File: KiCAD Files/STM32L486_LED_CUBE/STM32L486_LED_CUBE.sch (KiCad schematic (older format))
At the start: 0 parts

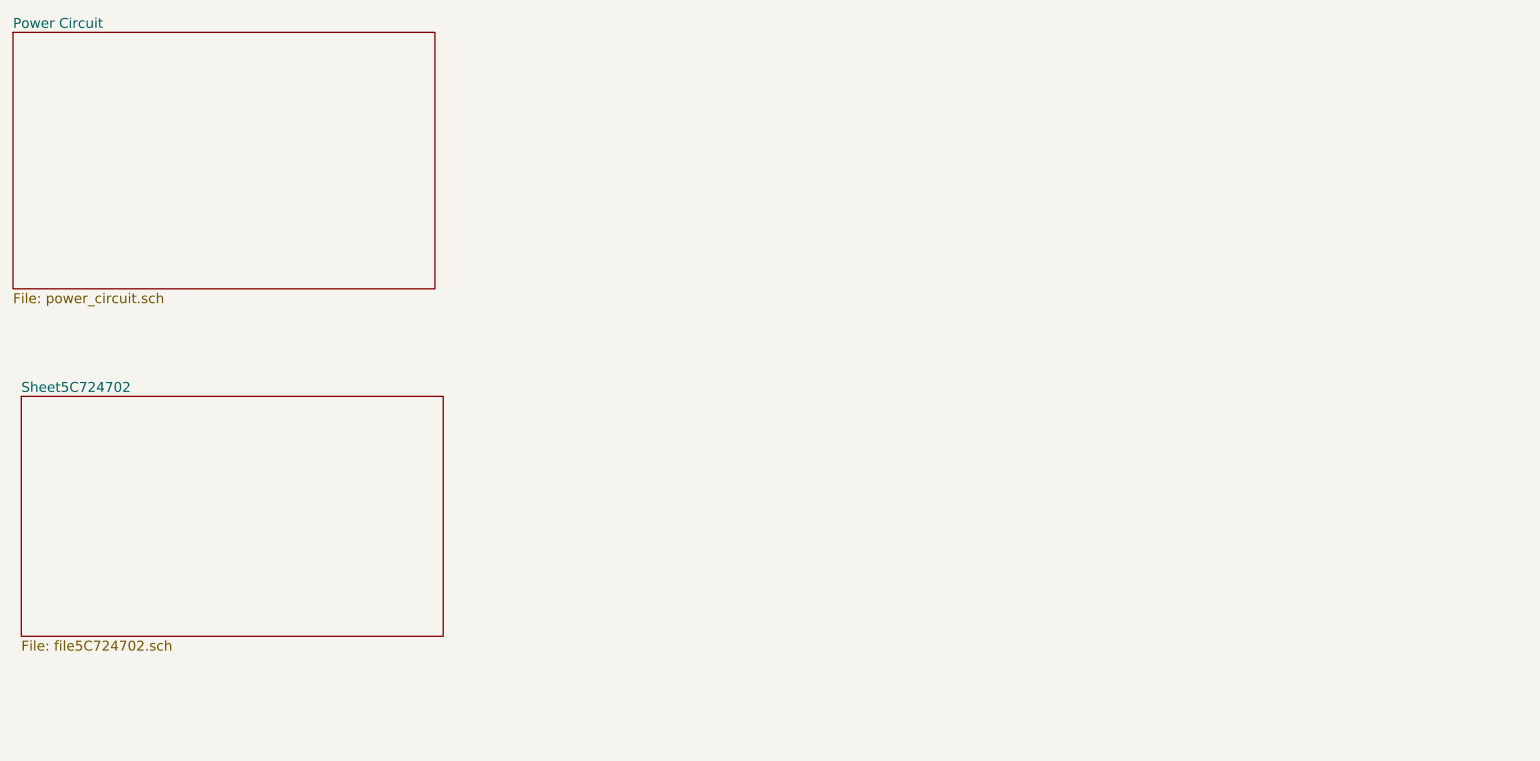
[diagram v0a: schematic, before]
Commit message: Updated KiCAD schematic. TLC portion added.
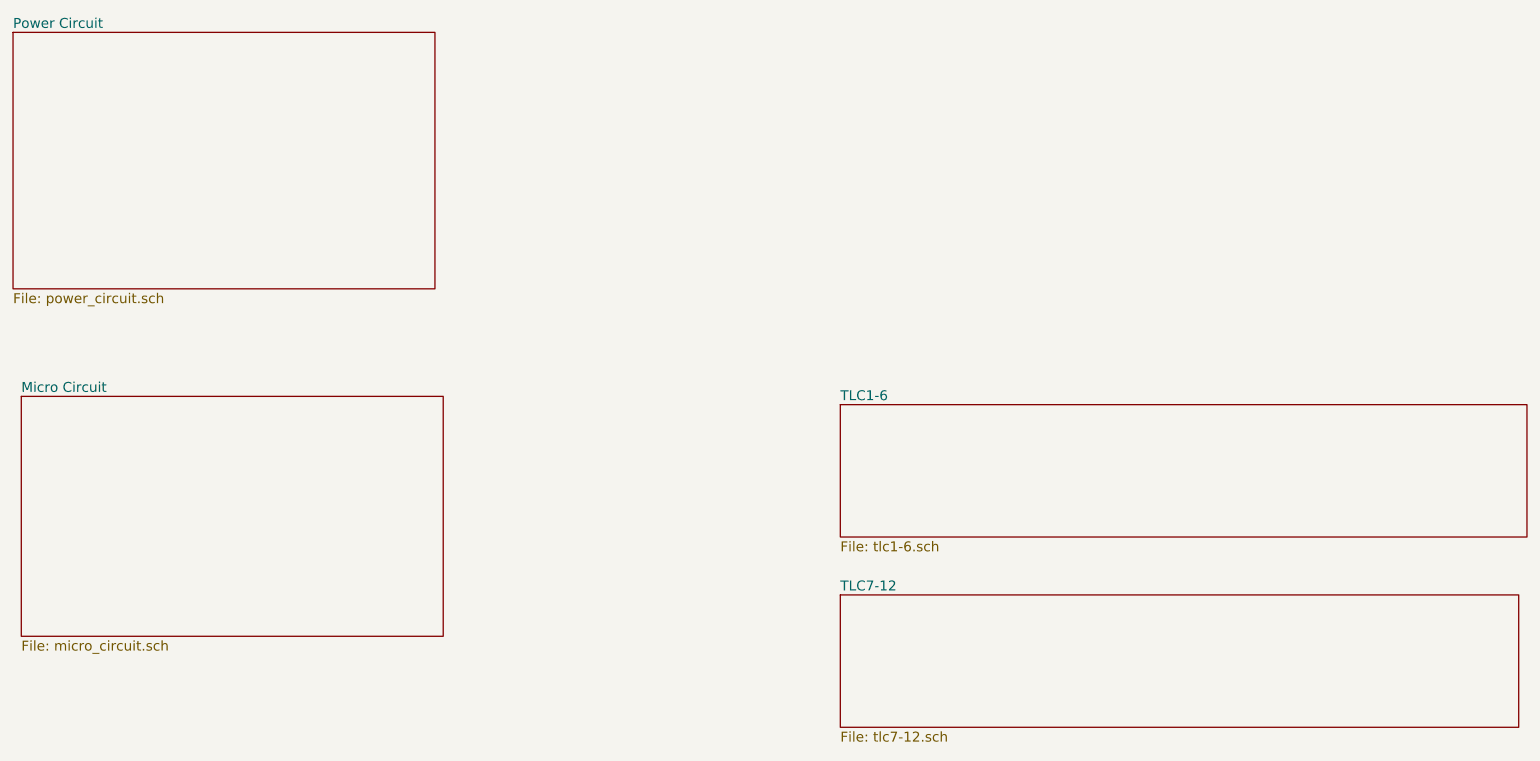
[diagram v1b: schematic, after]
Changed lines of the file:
@@
 $Descr A4 11693 8268
 encoding utf-8
-Sheet 1 3
+Sheet 1 5
 Title ""
 Date ""
@@
 S 1700 3300 2550 1450
 U 5C724703
-F0 "Sheet5C724702" 60
-F1 "file5C724702.sch" 60
+F0 "Micro Circuit" 60
+F1 "micro_circuit.sch" 60
+$EndSheet
+$Sheet
+S 6650 3350 4150 800
+U 5C733F59
+F0 "TLC1-6" 60
+F1 "tlc1-6.sch" 60
+$EndSheet
+$Sheet
+S 6650 4500 4100 800
+U 5C7476A3
+F0 "TLC7-12" 60
+F1 "tlc7-12.sch" 60
 $EndSheet
 $EndSCHEMATC
